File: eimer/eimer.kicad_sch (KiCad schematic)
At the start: 21 parts, among them J2 USB_C_Receptacle_USB2.0_14P, U1 RP2040, U2 NCP1117-3.3_SOT223

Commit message: more work on schematic
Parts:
- added C15, C16: 15pF, symbol Device:C
- added C17: 0.1uF, symbol Device:C
- added J1: Conn_01x20, symbol Connector_Generic:Conn_01x20
- added J2: Conn_01x20, Connector_PinHeader_2.54mm:PinHeader_1x20_P2.54mm_Vertical, symbol Connector_Generic:Conn_01x20
- added J3: Conn_01x03, Connector_PinHeader_2.54mm:PinHeader_1x03_P2.54mm_Vertical, symbol Connector_Generic:Conn_01x03
- added R5, R6: 1K, symbol Device:R
- added R7: 10K, symbol Device:R
- added SW1: SW_Push, symbol Switch:SW_Push
- added U3: W25Q128JVS, Package_SO:SOIC-8_5.3x5.3mm_P1.27mm, symbol Memory_Flash:W25Q128JVS
- added Y1: 12 MHz, Crystal:Crystal_SMD_3225-4Pin_3.2x2.5mm, symbol Device:Crystal_GND24
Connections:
- net +3.3V: now also C17.1, R7.2, U3.8 (VCC)
- net GND: now also U1.19 (TESTEN), C15.1, C16.2, C17.2, SW1.1, U3.4 (GND), Y1.2, Y1.4
- net XIN: now also C15.2, Y1.3
- net XOUT: now also R5.2
- net GPIO8: now reaches U1.11 (GPIO8)
- net GPIO9: now reaches U1.12 (GPIO9)
- net GPIO10: now reaches U1.13 (GPIO10)
- net GPIO11: now reaches U1.14 (GPIO11)
- net GPIO12: now reaches U1.15 (GPIO12)
- net GPIO13: now reaches U1.16 (GPIO13)
- net GPIO14: now reaches U1.17 (GPIO14)
- net GPIO15: now reaches U1.18 (GPIO15)
- net GPIO0: now reaches U1.2 (GPIO0)
- net GPIO0: now also J1.1 (Pin_1)
- net SWCLK: now reaches U1.24 (SWCLK)
- net SWDIO: now reaches U1.25 (SWDIO)
- net RUN: now reaches U1.26 (RUN)
- net GPIO16: now reaches U1.27 (GPIO16)
- net GPIO17: now reaches U1.28 (GPIO17)
- net GPIO18: now reaches U1.29 (GPIO18)
- net GPIO1: now reaches U1.3 (GPIO1)
- net GPIO1: now also J1.2 (Pin_2)
- net GPIO19: now reaches U1.30 (GPIO19)
- net GPIO20: now reaches U1.31 (GPIO20)
- net GPIO21: now reaches U1.32 (GPIO21)
- net GPIO22: now reaches U1.34 (GPIO22)
- net GPIO23: now reaches U1.35 (GPIO23)
- net GPIO24: now reaches U1.36 (GPIO24)
- net GPIO25: now reaches U1.37 (GPIO25)
- net GPIO26/ADC0: now reaches U1.38 (GPIO26/ADC0)
- net GPIO27/ADC1: now reaches U1.39 (GPIO27/ADC1)
- net GPIO2: now reaches U1.4 (GPIO2)
- net GPIO2: now also J1.4 (Pin_4)
- net GPIO28/ADC2: now reaches U1.40 (GPIO28/ADC2)
- net GPIO29/ADC3: now reaches U1.41 (GPIO29/ADC3)
- net GPIO3: now reaches U1.5 (GPIO3)
- net GPIO3: now also J1.5 (Pin_5)
- net QSPI_SD3: now reaches U1.51 (QSPI_SD3)
- net QSPI_SD3: now also U3.7 (~{HOLD}/~{RESET}/IO_{3})
- net QSPI_SCLK: now reaches U1.52 (QSPI_SCLK)
- net QSPI_SCLK: now also U3.6 (CLK)
- net QSPI_SD0: now reaches U1.53 (QSPI_SD0)
- net QSPI_SD0: now also U3.5 (DI/IO_{0})
- net QSPI_SD2: now reaches U1.54 (QSPI_SD2)
- net QSPI_SD2: now also U3.3 (~{WP}/IO_{2})
- net QSPI_SD1: now reaches U1.55 (QSPI_SD1)
- net QSPI_SD1: now also U3.2 (DO/IO_{1})
- net QSPI_SS: now reaches U1.56 (~{QSPI_SS})
- net QSPI_SS: now also R6.2, R7.1, U3.1 (~{CS})
- net GPIO4: now reaches U1.6 (GPIO4)
- net GPIO4: now also J1.6 (Pin_6)
- net GPIO5: now reaches U1.7 (GPIO5)
- net GPIO5: now also J1.7 (Pin_7)
- net GPIO6: now reaches U1.8 (GPIO6)
- net GPIO7: now reaches U1.9 (GPIO7)
- new net: R6.1, SW1.2
- new net: C16.1, R5.1, Y1.1
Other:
- moved on the sheet: C1, C10, C11, C12, C13, C14, C2, C3, C4, C5, C6, C7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

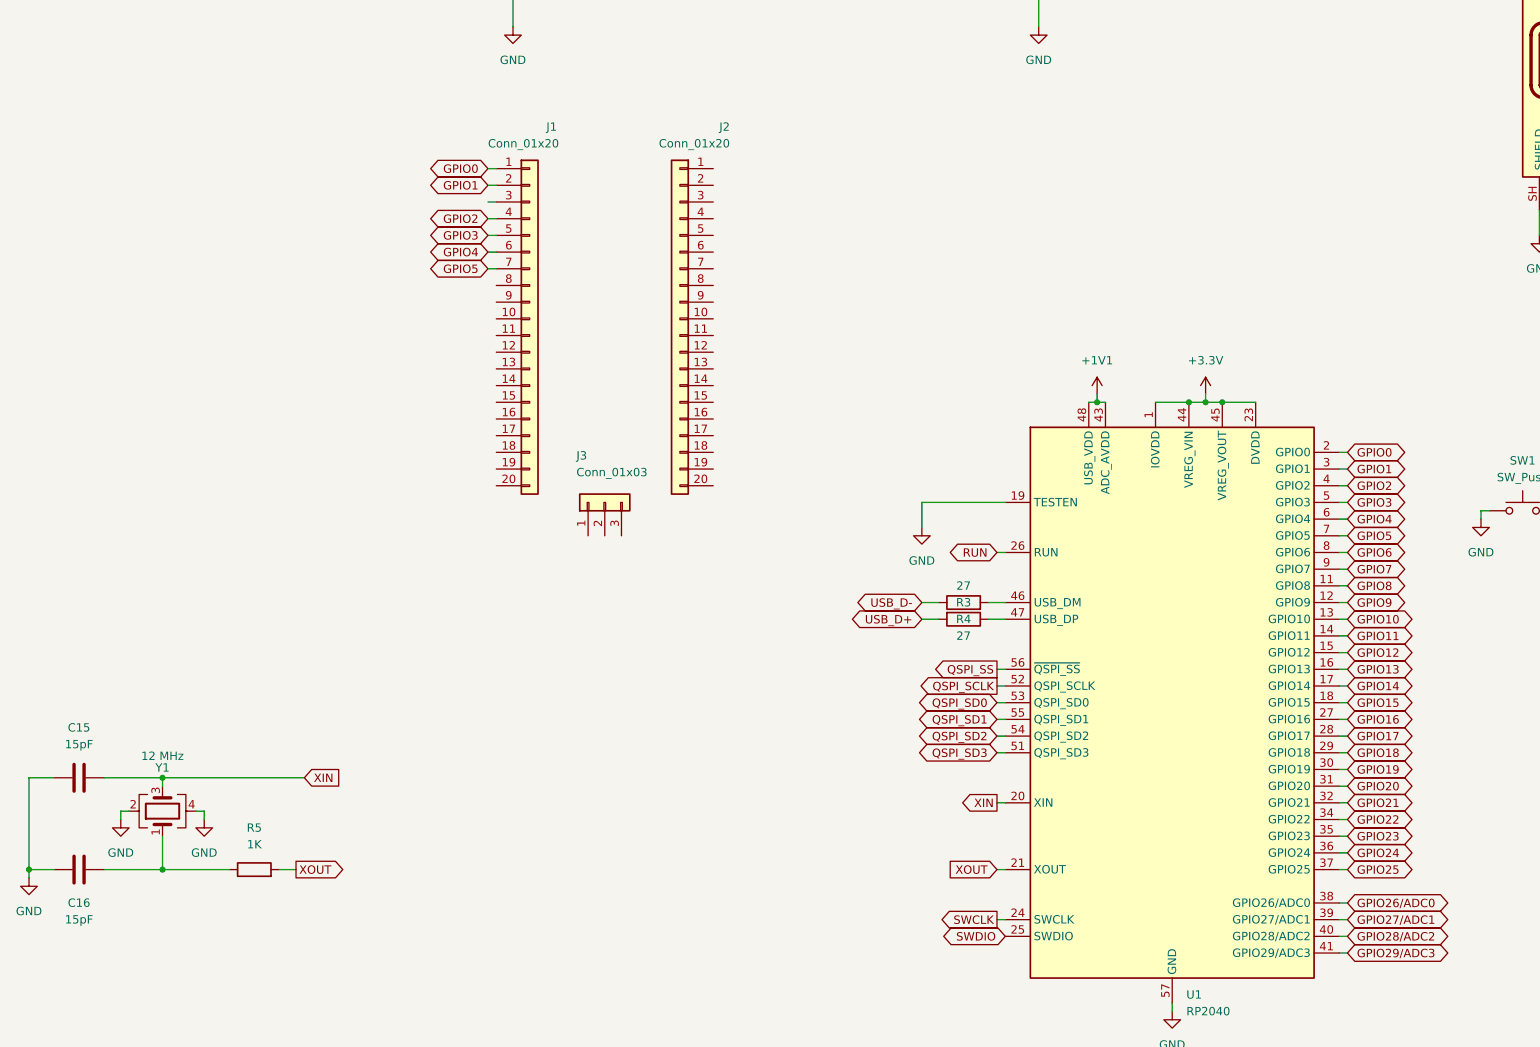
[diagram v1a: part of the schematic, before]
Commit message: finished schematic according to guide
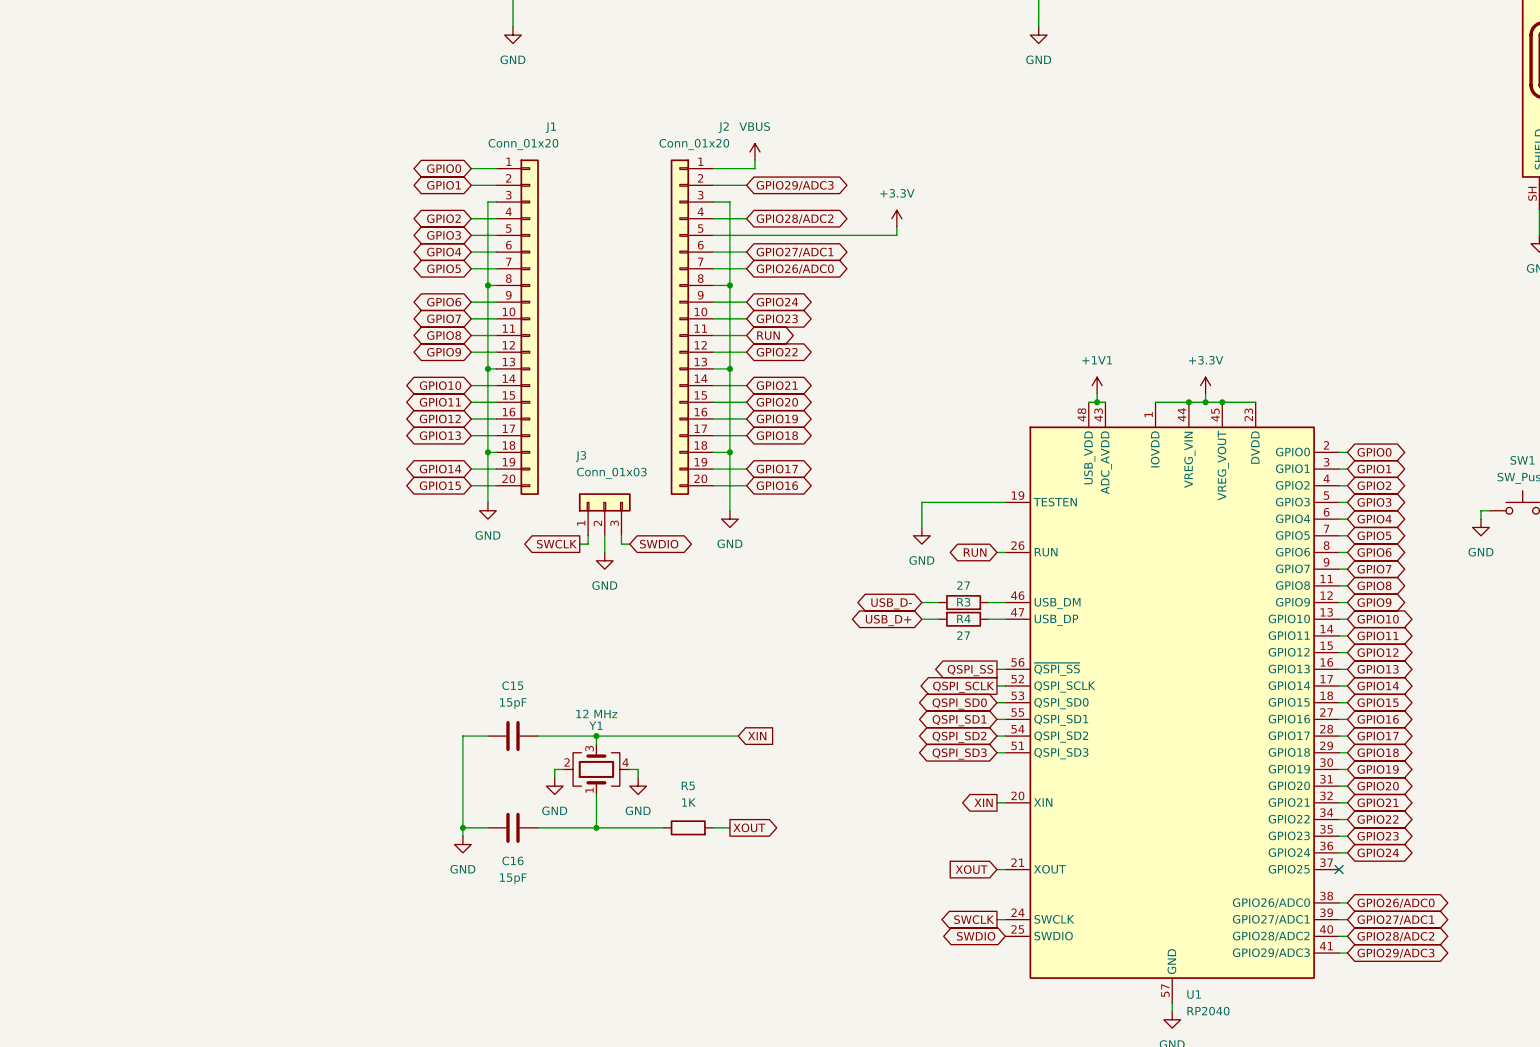
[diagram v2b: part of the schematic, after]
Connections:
- net +3.3V: now also J2.5 (Pin_5)
- net GND: now also J1.13 (Pin_13), J1.18 (Pin_18), J1.3 (Pin_3), J1.8 (Pin_8), J2.13 (Pin_13), J2.18 (Pin_18), J2.3 (Pin_3), J2.8 (Pin_8), J3.2 (Pin_2)
- net GPIO10: now also J1.14 (Pin_14)
- net GPIO11: now also J1.15 (Pin_15)
- net GPIO12: now also J1.16 (Pin_16)
- net GPIO13: now also J1.17 (Pin_17)
- net GPIO14: now also J1.19 (Pin_19)
- net GPIO15: now also J1.20 (Pin_20)
- net GPIO16: now also J2.20 (Pin_20)
- net GPIO17: now also J2.19 (Pin_19)
- net GPIO18: now also J2.17 (Pin_17)
- net GPIO19: now also J2.16 (Pin_16)
- net GPIO20: now also J2.15 (Pin_15)
- net GPIO21: now also J2.14 (Pin_14)
- net GPIO22: now also J2.12 (Pin_12)
- net GPIO23: now also J2.10 (Pin_10)
- net GPIO24: now also J2.9 (Pin_9)
- net GPIO26/ADC0: now also J2.7 (Pin_7)
- net GPIO27/ADC1: now also J2.6 (Pin_6)
- net GPIO28/ADC2: now also J2.4 (Pin_4)
- net GPIO29/ADC3: now also J2.2 (Pin_2)
- net GPIO6: now also J1.9 (Pin_9)
- net GPIO7: now also J1.10 (Pin_10)
- net GPIO8: now also J1.11 (Pin_11)
- net GPIO9: now also J1.12 (Pin_12)
- net RUN: now also J2.11 (Pin_11)
- net SWCLK: now also J3.1 (Pin_1)
- net SWDIO: now also J3.3 (Pin_3)
- net VBUS: now also J2.1 (Pin_1)
- net GPIO25: no longer names the net of U1.37 (GPIO25)
- no-connect marks 0 -> 1
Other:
- moved on the sheet: C15, C16, R5, Y1

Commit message: assigned footprints according to docs
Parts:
- C1, C10, C11, C12, C17, C2, C3, C4, C5, C6, C7, C8, C9: footprint (none) -> Capacitor_SMD:C_0402_1005Metric
- C13, C14: footprint (none) -> Capacitor_SMD:C_0603_1608Metric
- C15, C16: value 15pF -> 33pF; footprint (none) -> Capacitor_SMD:C_0402_1005Metric
- J1: footprint (none) -> Connector_PinHeader_2.54mm:PinHeader_1x20_P2.54mm_Vertical
- J4: renamed from J2; footprint (none) -> Connector_USB:USB_C_Receptacle_HRO_TYPE-C-31-M-12
- R1, R2, R3, R4, R5, R6, R7: footprint (none) -> Resistor_SMD:R_0402_1005Metric
- SW1: footprint (none) -> Button_Switch_SMD:SW_Push_SPST_NO_Alps_SKRK
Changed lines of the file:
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@@
 			)
 		)
-		(property "Footprint" ""
+		(property "Footprint" "Capacitor_SMD:C_0402_1005Metric"
 			(at 73.3552 38.1 0)
 			(hide yes)
@@
 			)
 		)
-		(property "Footprint" ""
+		(property "Footprint" "Capacitor_SMD:C_0402_1005Metric"
 			(at 61.9252 38.1 0)
 			(hide yes)
@@
 			)
 		)
-		(property "Footprint" ""
+		(property "Footprint" "Capacitor_SMD:C_0603_1608Metric"
 			(at 234.6452 40.64 0)
 			(hide yes)
@@
 			)
 		)
-		(property "Footprint" ""
+		(property "Footprint" "Resistor_SMD:R_0402_1005Metric"
 			(at 215.9 38.862 90)
 			(hide yes)
@@
 			)
 		)
-		(property "Footprint" ""
+		(property "Footprint" "Capacitor_SMD:C_0402_1005Metric"
 			(at 238.76 108.2548 0)
 			(hide yes)
@@
 			)
 		)
-		(property "Footprint" ""
+		(property "Footprint" "Resistor_SMD:R_0402_1005Metric"
 			(at 99.06 131.572 90)
 			(hide yes)
@@
 		(dnp no)
 		(fields_autoplaced yes)
-		(property "Reference" "J2"
+		(property "Reference" "J4"
 			(at 194.31 25.4 0)
 			(show_name no)
@@
 			)
 		)
-		(property "Footprint" ""
+		(property "Footprint" "Connector_USB:USB_C_Receptacle_HRO_TYPE-C-31-M-12"
 			(at 198.12 48.26 0)
 			(hide yes)
@@
 			(project "eimer"
 				(path "/310aac61-9967-4677-964a-8a6056e13ca2"
-					(reference "J2")
+					(reference "J4")
 					(unit 1)
 				)
@@
 			)
 		)
-		(property "Footprint" ""
+		(property "Footprint" "Button_Switch_SMD:SW_Push_SPST_NO_Alps_SKRK"
 			(at 184.15 111.76 0)
 			(hide yes)
@@
 			)
 		)
-		(property "Footprint" ""
+		(property "Footprint" "Resistor_SMD:R_0402_1005Metric"
 			(at 203.708 110.49 90)
 			(hide yes)
@@
 			)
 		)
-		(property "Footprint" ""
+		(property "Footprint" "Resistor_SMD:R_0402_1005Metric"
 			(at 194.31 118.618 90)
 			(hide yes)
@@
 			)
 		)
-		(property "Value" "15pF"
+		(property "Value" "33pF"
 			(at 30.48 146.05 90)
 			(show_name no)
@@
 			)
 		)
-		(property "Footprint" ""
+		(property "Footprint" "Capacitor_SMD:C_0402_1005Metric"
 			(at 34.29 150.1648 0)
 			(hide yes)
@@
 			)
 		)
-		(property "Footprint" ""
+		(property "Footprint" "Connector_PinHeader_2.54mm:PinHeader_1x20_P2.54mm_Vertical"
 			(at 33.02 87.63 0)
 			(hide yes)
@@
 			)
 		)
-		(property "Footprint" ""
+		(property "Footprint" "Capacitor_SMD:C_0402_1005Metric"
 			(at 44.1452 38.1 0)
 			(hide yes)
@@
 			)
 		)
-		(property "Footprint" ""
+		(property "Footprint" "Capacitor_SMD:C_0402_1005Metric"
 			(at 136.8552 38.1 0)
 			(hide yes)
@@
 			)
 		)
-		(property "Footprint" ""
+		(property "Footprint" "Capacitor_SMD:C_0402_1005Metric"
 			(at 31.4452 38.1 0)
 			(hide yes)
@@
 			)
 		)
-		(property "Footprint" ""
+		(property "Footprint" "Capacitor_SMD:C_0402_1005Metric"
 			(at 149.5552 38.1 0)
 			(hide yes)
@@
 			)
 		)
-		(property "Footprint" ""
+		(property "Footprint" "Capacitor_SMD:C_0402_1005Metric"
 			(at 162.2552 38.1 0)
 			(hide yes)
@@
 			)
 		)
-		(property "Footprint" ""
+		(property "Footprint" "Capacitor_SMD:C_0402_1005Metric"
 			(at 20.0152 38.1 0)
 			(hide yes)
@@
 			)
 		)
-		(property "Footprint" ""
+		(property "Footprint" "Capacitor_SMD:C_0402_1005Metric"
 			(at 98.7552 38.1 0)
 			(hide yes)
@@
 			)
 		)
-		(property "Footprint" ""
+		(property "Footprint" "Resistor_SMD:R_0402_1005Metric"
 			(at 215.9 39.878 90)
 			(hide yes)
@@
 			)
 		)
-		(property "Footprint" ""
+		(property "Footprint" "Resistor_SMD:R_0402_1005Metric"
 			(at 99.06 132.588 90)
 			(hide yes)
@@
 			)
 		)
-		(property "Footprint" ""
+		(property "Footprint" "Capacitor_SMD:C_0603_1608Metric"
 			(at 263.8552 40.64 0)
 			(hide yes)
@@
 			)
 		)
-		(property "Footprint" ""
+		(property "Footprint" "Resistor_SMD:R_0402_1005Metric"
 			(at 57.15 166.878 90)
 			(hide yes)
@@
 			)
 		)
-		(property "Footprint" ""
+		(property "Footprint" "Capacitor_SMD:C_0402_1005Metric"
 			(at 86.0552 38.1 0)
 			(hide yes)
@@
 			)
 		)
-		(property "Value" "15pF"
+		(property "Value" "33pF"
 			(at 30.48 172.72 90)
 			(show_name no)
@@
 			)
 		)
-		(property "Footprint" ""
+		(property "Footprint" "Capacitor_SMD:C_0402_1005Metric"
 			(at 26.67 166.0652 0)
 			(hide yes)
@@
 			)
 		)
-		(property "Footprint" ""
+		(property "Footprint" "Capacitor_SMD:C_0402_1005Metric"
 			(at 124.1552 38.1 0)
 			(hide yes)
@@
 			)
 		)
-		(property "Footprint" ""
+		(property "Footprint" "Capacitor_SMD:C_0402_1005Metric"
 			(at 111.4552 38.1 0)
 			(hide yes)
